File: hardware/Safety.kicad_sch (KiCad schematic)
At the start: 5 parts, among them K1 FINDER-30.22, Q1 BSS138

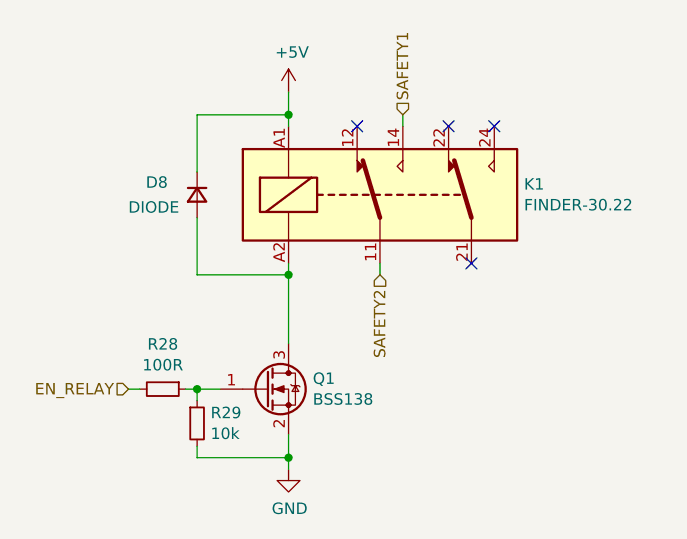
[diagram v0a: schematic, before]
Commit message: Add brake pressure sensors
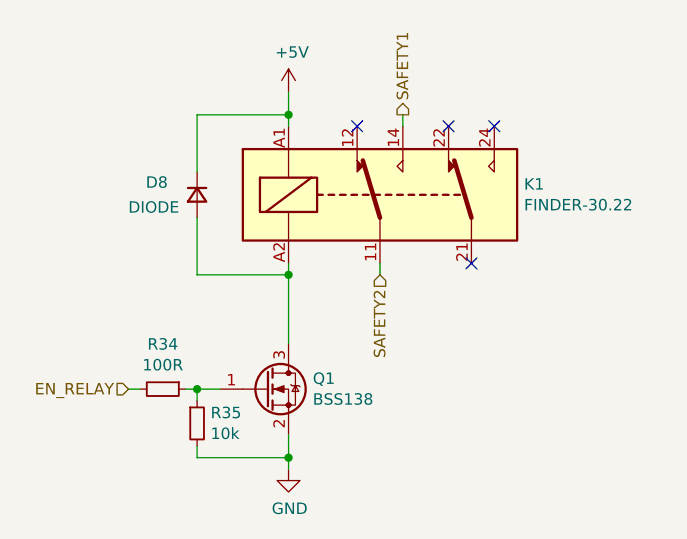
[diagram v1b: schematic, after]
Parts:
- renumbered R28 to R34, R29 to R35
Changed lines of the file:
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@@
     (effects (font (size 1.27 1.27)) (justify right))
   )
-  (hierarchical_label "SAFETY1" (shape input) (at 156.21 82.55 90) (fields_autoplaced)
+  (hierarchical_label "SAFETY1" (shape output) (at 156.21 82.55 90) (fields_autoplaced)
     (effects (font (size 1.27 1.27)) (justify left))
   )
@@
   (symbol (lib_id "Device:R_Small") (at 129.54 113.03 270) (unit 1)
     (in_bom yes) (on_board yes) (dnp no)
-    (property "Reference" "R28" (at 129.54 108.0516 90)
+    (property "Reference" "R34" (at 129.54 108.0516 90)
       (effects (font (size 1.27 1.27)))
     )
@@
       (project "APPS"
         (path "/fc4ad874-c922-4070-89f9-7262080469d8/00000000-0000-0000-0000-00005f99e99e"
-          (reference "R28") (unit 1)
+          (reference "R34") (unit 1)
         )
       )
@@
   (symbol (lib_id "Device:R_Small") (at 133.35 116.84 0) (unit 1)
     (in_bom yes) (on_board yes) (dnp no)
-    (property "Reference" "R29" (at 134.8486 115.6716 0)
+    (property "Reference" "R35" (at 134.8486 115.6716 0)
       (effects (font (size 1.27 1.27)) (justify left))
     )
@@
       (project "APPS"
         (path "/fc4ad874-c922-4070-89f9-7262080469d8/00000000-0000-0000-0000-00005f99e99e"
-          (reference "R29") (unit 1)
+          (reference "R35") (unit 1)
         )
       )
@@
   (symbol (lib_id "power:+5V") (at 143.51 80.01 0) (unit 1)
     (in_bom yes) (on_board yes) (dnp no)
-    (property "Reference" "#PWR048" (at 143.51 83.82 0)
+    (property "Reference" "#PWR055" (at 143.51 83.82 0)
       (effects (font (size 1.27 1.27)) hide)
     )
@@
       (project "APPS"
         (path "/fc4ad874-c922-4070-89f9-7262080469d8/00000000-0000-0000-0000-00005f99e99e"
-          (reference "#PWR048") (unit 1)
+          (reference "#PWR055") (unit 1)
         )
       )
@@
   (symbol (lib_id "power:GND") (at 143.51 121.92 0) (unit 1)
     (in_bom yes) (on_board yes) (dnp no)
-    (property "Reference" "#PWR049" (at 143.51 128.27 0)
+    (property "Reference" "#PWR056" (at 143.51 128.27 0)
       (effects (font (size 1.27 1.27)) hide)
     )
@@
       (project "APPS"
         (path "/fc4ad874-c922-4070-89f9-7262080469d8/00000000-0000-0000-0000-00005f99e99e"
-          (reference "#PWR049") (unit 1)
+          (reference "#PWR056") (unit 1)
         )
       )
